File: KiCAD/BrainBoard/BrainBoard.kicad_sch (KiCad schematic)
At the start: 2 parts, among them J1 Battery Input

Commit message: feat: battery input
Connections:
- net +12V renamed +BATT
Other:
- sheet Voltage Regulator ports: added BATT; removed 12V
- note added: "3S, 12V nominal TLV1117-33 restricts battery to max. 15V"
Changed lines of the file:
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@@
 		(company "Nathan Wignall, Minh Nguyen, Ana Wise")
+	)
+	(text "3S, 12V nominal\nTLV1117-33 restricts battery to max. 15V"
+		(exclude_from_sim no)
+		(at 31.75 64.77 0)
+		(effects
+			(font
+				(size 1.27 1.27)
+			)
+		)
 	)
 	(junction
@@
 			)
 		)
-		(property "Value" "+12V"
+		(property "Value" "+BATT"
 			(at 38.1 68.58 0)
 			(effects
@@
 		(on_board yes)
 		(dnp no)
-		(fields_autoplaced yes)
 		(property "Reference" "#PWR09"
 			(at 175.26 67.31 0)
@@
 			)
 		)
-		(property "Value" "+12V"
-			(at 175.26 58.42 0)
-			(effects
-				(font
-					(size 1.27 1.27)
-				)
+		(property "Value" "+BATT"
+			(at 172.72 58.674 0)
+			(effects
+				(font
+					(size 1.27 1.27)
+				)
+				(justify left)
 			)
 		)
@@
 			)
 		)
-		(property "Value" "+12V"
+		(property "Value" "+BATT"
 			(at 55.88 69.85 0)
 			(effects
@@
 			)
 		)
-		(pin "12V" input
+		(pin "BATT" input
 			(at 58.42 90.17 180)
 			(effects

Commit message: fix: correct nominal voltage
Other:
- note added: "3S, 11.1V nominal TLV1117-33 restricts battery to max. 15V"
- note removed: "3S, 12V nominal TLV1117-33 restricts battery to max. 15V"
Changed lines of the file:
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@@
 		(company "Nathan Wignall, Minh Nguyen, Ana Wise")
 	)
-	(text "3S, 12V nominal\nTLV1117-33 restricts battery to max. 15V"
+	(text "3S, 11.1V nominal\nTLV1117-33 restricts battery to max. 15V"
 		(exclude_from_sim no)
 		(at 31.75 64.77 0)

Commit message: feat: added hiearchal power pins to microcontroller to avoid having global labels in hiearchal sheets
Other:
- sheet STM32F303CCT6 Microcontroller ports: added 3.3V, 3.3VA, PB8_IN; removed none
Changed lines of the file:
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@@
+	(wire
+		(pts
+			(xy 120.65 88.9) (xy 121.92 88.9)
+		)
+		(stroke
+			(width 0)
+			(type default)
+		)
+	)
 	(wire
 		(pts
@@
 		(pts
 			(xy 55.88 90.17) (xy 58.42 90.17)
+		)
+		(stroke
+			(width 0)
+			(type default)
+		)
+	)
+	(wire
+		(pts
+			(xy 120.65 92.075) (xy 121.92 92.075)
 		)
 		(stroke
@@
 	)
 	(symbol
+		(lib_id "power:+3.3V")
+		(at 120.65 88.9 90)
+		(unit 1)
+		(exclude_from_sim no)
+		(in_bom yes)
+		(on_board yes)
+		(dnp no)
+		(fields_autoplaced yes)
+		(property "Reference" "#PWR016"
+			(at 124.46 88.9 0)
+			(effects
+				(font
+					(size 1.27 1.27)
+				)
+				(hide yes)
+			)
+		)
+		(property "Value" "+3.3V"
+			(at 117.475 88.8999 90)
+			(effects
+				(font
+					(size 1.27 1.27)
+				)
+				(justify left)
+			)
+		)
+		(property "Footprint" ""
+			(at 120.65 88.9 0)
+			(effects
+				(font
+					(size 1.27 1.27)
+				)
+				(hide yes)
+			)
+		)
+		(property "Datasheet" ""
+			(at 120.65 88.9 0)
+			(effects
+				(font
+					(size 1.27 1.27)
+				)
+				(hide yes)
+			)
+		)
+		(property "Description" "Power symbol creates a global label with name \"+3.3V\""
+			(at 120.65 88.9 0)
+			(effects
+				(font
+					(size 1.27 1.27)
+				)
+				(hide yes)
+			)
+		)
+		(pin "1"
+		)
+		(instances
+			(project "BrainBoard"
+				(path "/44e391a9-9312-4881-bf0a-d93a44472e34"
+					(reference "#PWR016")
+					(unit 1)
+				)
+			)
+		)
+	)
+	(symbol
 		(lib_id "power:GND")
 		(at 38.1 86.36 0)
@@
 		)
 	)
+	(symbol
+		(lib_id "power:+3.3VA")
+		(at 120.65 92.075 90)
+		(unit 1)
+		(exclude_from_sim no)
+		(in_bom yes)
+		(on_board yes)
+		(dnp no)
+		(property "Reference" "#PWR018"
+			(at 124.46 92.075 0)
+			(effects
+				(font
+					(size 1.27 1.27)
+				)
+				(hide yes)
+			)
+		)
+		(property "Value" "+3.3VA"
+			(at 117.475 92.075 90)
+			(effects
+				(font
+					(size 1.27 1.27)
+				)
+				(justify left)
+			)
+		)
+		(property "Footprint" ""
+			(at 120.65 92.075 0)
+			(effects
+				(font
+					(size 1.27 1.27)
+				)
+				(hide yes)
+			)
+		)
+		(property "Datasheet" ""
+			(at 120.65 92.075 0)
+			(effects
+				(font
+					(size 1.27 1.27)
+				)
+				(hide yes)
+			)
+		)
+		(property "Description" "Power symbol creates a global label with name \"+3.3VA\""
+			(at 120.65 92.075 0)
+			(effects
+				(font
+					(size 1.27 1.27)
+				)
+				(hide yes)
+			)
+		)
+		(pin "1"
+		)
+		(instances
+			(project ""
+				(path "/44e391a9-9312-4881-bf0a-d93a44472e34"
+					(reference "#PWR018")
+					(unit 1)
+				)
+			)
+		)
+	)
 	(sheet
 		(at 58.42 81.28)
@@
 			)
 		)
+		(pin "PB8_IN" input
+			(at 121.92 64.77 180)
+			(effects
+				(font
+					(size 1.27 1.27)
+				)
+				(justify left)
+			)
+		)
+		(pin "3.3V" input
+			(at 121.92 88.9 180)
+			(effects
+				(font
+					(size 1.27 1.27)
+				)
+				(justify left)
+			)
+		)
+		(pin "3.3VA" output
+			(at 121.92 92.075 180)
+			(effects
+				(font
+					(size 1.27 1.27)
+				)
+				(justify left)
+			)
+		)

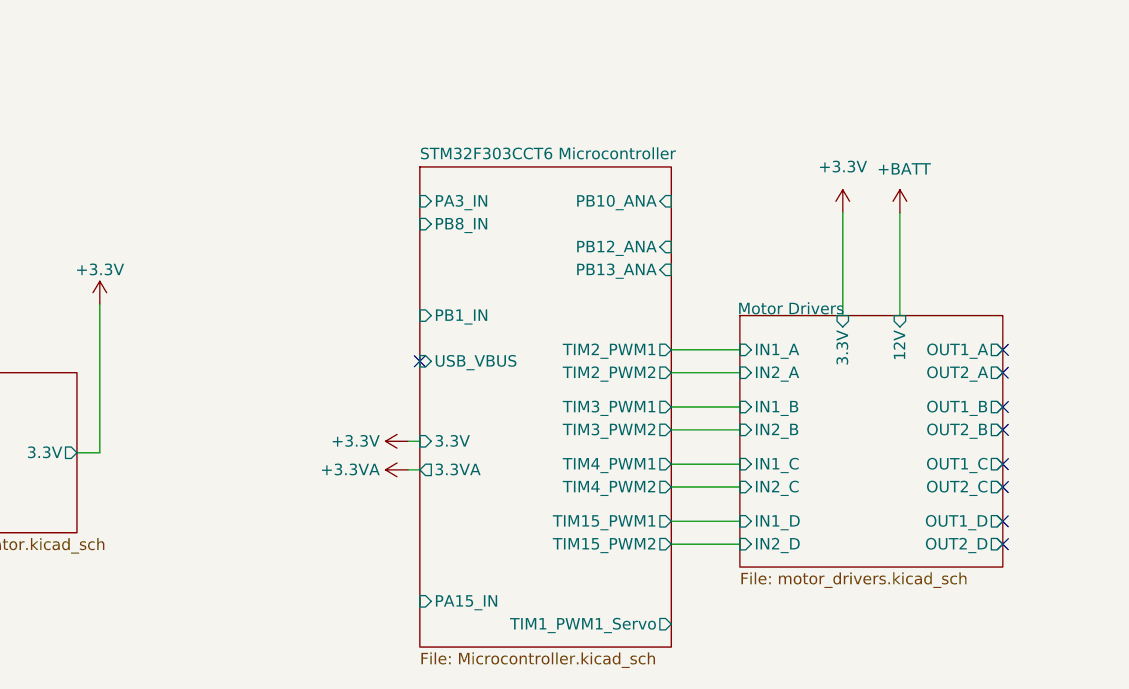
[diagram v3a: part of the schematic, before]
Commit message: feat: added micro-jst connector pins for distance sensors
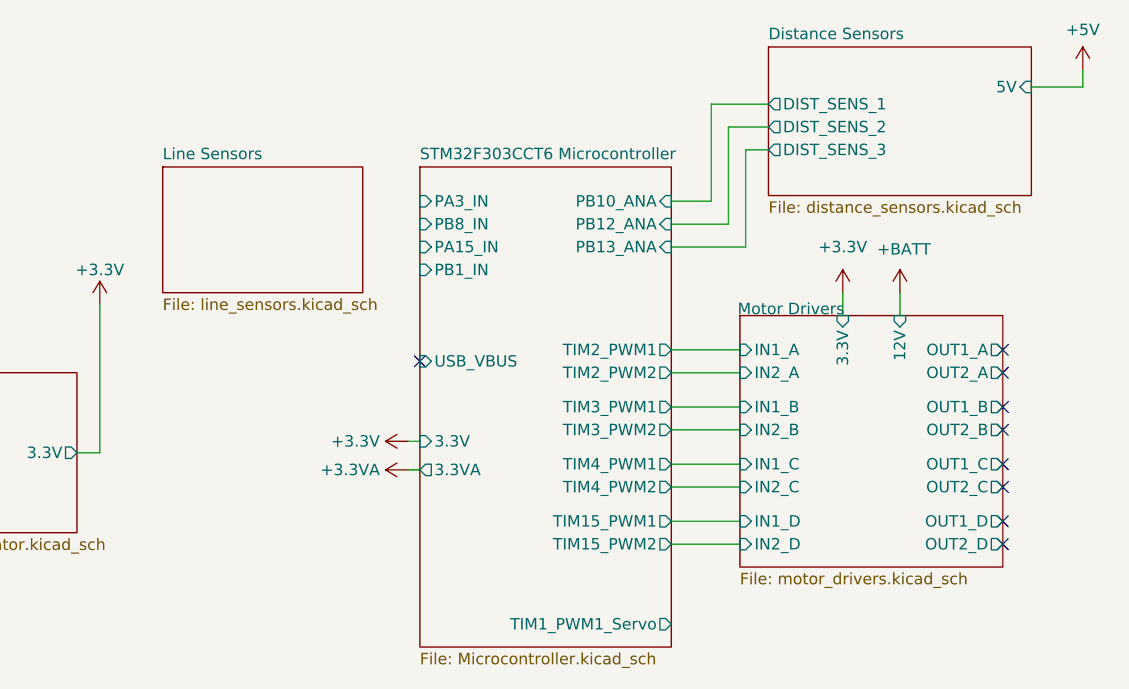
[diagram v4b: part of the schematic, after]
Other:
- added sheet Distance Sensors (distance_sensors.kicad_sch)
- added sheet Line Sensors (line_sensors.kicad_sch)

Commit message: feat: Line sensor thing push
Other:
- sheet Line Sensors ports: added 3V3, LINE_1, LINE_2, LINE_3, LINE_4; removed none
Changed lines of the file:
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@@
+	(wire
+		(pts
+			(xy 115.57 67.31) (xy 121.92 67.31)
+		)
+		(stroke
+			(width 0)
+			(type default)
+		)
+	)
 	(wire
 		(pts
@@
 	(wire
 		(pts
+			(xy 87.63 61.595) (xy 87.63 57.15)
+		)
+		(stroke
+			(width 0)
+			(type default)
+		)
+	)
+	(wire
+		(pts
 			(xy 86.36 73.66) (xy 86.36 90.17)
 		)
@@
 	(wire
 		(pts
+			(xy 115.57 64.77) (xy 121.92 64.77)
+		)
+		(stroke
+			(width 0)
+			(type default)
+		)
+	)
+	(wire
+		(pts
+			(xy 115.57 62.23) (xy 121.92 62.23)
+		)
+		(stroke
+			(width 0)
+			(type default)
+		)
+	)
+	(wire
+		(pts
 			(xy 149.86 81.28) (xy 157.48 81.28)
 		)
@@
 	(wire
 		(pts
+			(xy 93.345 61.595) (xy 87.63 61.595)
+		)
+		(stroke
+			(width 0)
+			(type default)
+		)
+	)
+	(wire
+		(pts
 			(xy 120.65 88.9) (xy 121.92 88.9)
 		)
@@
 		(pts
 			(xy 149.86 87.63) (xy 157.48 87.63)
+		)
+		(stroke
+			(width 0)
+			(type default)
+		)
+	)
+	(wire
+		(pts
+			(xy 115.57 69.85) (xy 121.92 69.85)
 		)
 		(stroke
@@
 	)
 	(symbol
+		(lib_id "power:+12V")
+		(at 87.63 57.15 0)
+		(unit 1)
+		(exclude_from_sim no)
+		(in_bom yes)
+		(on_board yes)
+		(dnp no)
+		(property "Reference" "#PWR031"
+			(at 87.63 60.96 0)
+			(effects
+				(font
+					(size 1.27 1.27)
+				)
+				(hide yes)
+			)
+		)
+		(property "Value" "+3.3V"
+			(at 87.63 53.34 0)
+			(effects
+				(font
+					(size 1.27 1.27)
+				)
+			)
+		)
+		(property "Footprint" ""
+			(at 87.63 57.15 0)
+			(effects
+				(font
+					(size 1.27 1.27)
+				)
+				(hide yes)
+			)
+		)
+		(property "Datasheet" ""
+			(at 87.63 57.15 0)
+			(effects
+				(font
+					(size 1.27 1.27)
+				)
+				(hide yes)
+			)
+		)
+		(property "Description" "Power symbol creates a global label with name \"+12V\""
+			(at 87.63 57.15 0)
+			(effects
+				(font
+					(size 1.27 1.27)
+				)
+				(hide yes)
+			)
+		)
+		(pin "1"
+		)
+		(instances
+			(project "BrainBoard"
+				(path "/44e391a9-9312-4881-bf0a-d93a44472e34"
+					(reference "#PWR031")
+					(unit 1)
+				)
+			)
+		)
+	)
+	(symbol
 		(lib_id "power:PWR_FLAG")
 		(at 38.1 72.39 90)
@@
 			)
 		)
+		(pin "LINE_3" output
+			(at 115.57 67.31 0)
+			(effects
+				(font
+					(size 1.27 1.27)
+				)
+				(justify right)
+			)
+		)
+		(pin "3V3" input
+			(at 93.345 61.595 180)
+			(effects
+				(font
+					(size 1.27 1.27)
+				)
+				(justify left)
+			)
+		)
+		(pin "LINE_2" output
+			(at 115.57 64.77 0)
+			(effects
+				(font
+					(size 1.27 1.27)
+				)
+				(justify right)
+			)
+		)
+		(pin "LINE_1" output
+			(at 115.57 62.23 0)
+			(effects
+				(font
+					(size 1.27 1.27)
+				)
+				(justify right)
+			)
+		)
+		(pin "LINE_4" output
+			(at 115.57 69.85 0)
+			(effects
+				(font
+					(size 1.27 1.27)
+				)
+				(justify right)
+			)
+		)
 		(instances
 			(project "BrainBoard"
@@
 		)
 		(pin "PB1_IN" input
-			(at 121.92 69.85 180)
+			(at 121.92 64.77 180)
 			(effects
 				(font
@@
 		)
 		(pin "PB8_IN" input
-			(at 121.92 64.77 180)
-			(effects
-				(font
+			(at 121.92 69.85 180)
+			(effects
+				(font

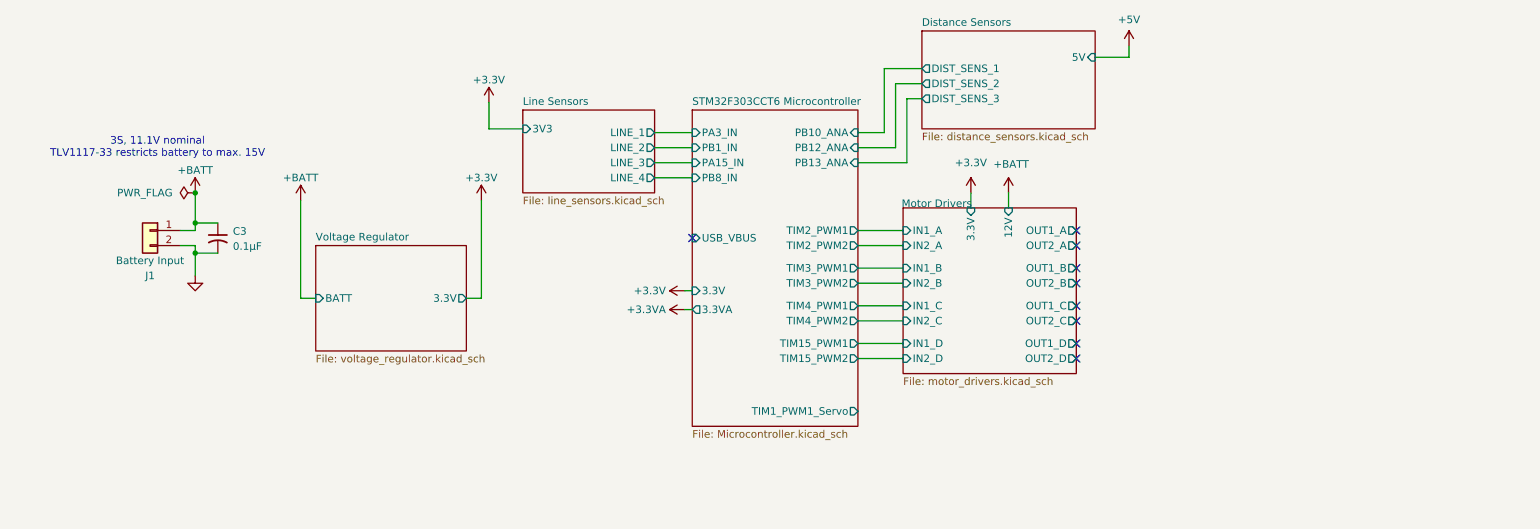
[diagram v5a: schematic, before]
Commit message: feat: add +5V line
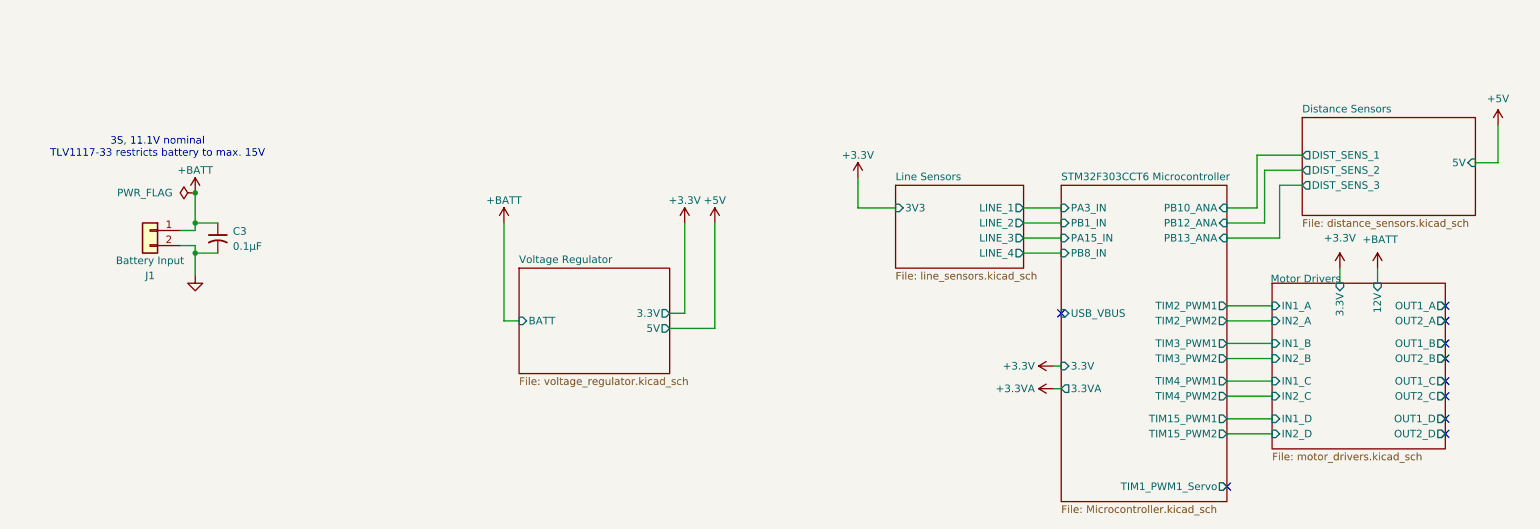
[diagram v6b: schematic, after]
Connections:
- no-connect marks 9 -> 10
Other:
- sheet Voltage Regulator ports: added 5V; removed none

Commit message: Assigned most general footprints
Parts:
- C3: footprint (none) -> Capacitor_SMD:C_0805_2012Metric
- J1: footprint (none) -> Connector_AMASS:AMASS_XT30U-M_1x02_P5.0mm_Vertical
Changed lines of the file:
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@@
 			)
 		)
-		(property "Footprint" ""
+		(property "Footprint" "Connector_AMASS:AMASS_XT30U-M_1x02_P5.0mm_Vertical"
 			(at 30.48 78.74 0)
 			(effects
@@
 			)
 		)
-		(property "Footprint" ""
+		(property "Footprint" "Capacitor_SMD:C_0805_2012Metric"
 			(at 41.91 80.01 0)
 			(effects
